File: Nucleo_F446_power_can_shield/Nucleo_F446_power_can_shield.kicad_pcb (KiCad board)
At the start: 2 copper layers, 70 x 59 mm, 2 parts, among them CN10 Conn_02x19_Odd_Even, CN7 Conn_02x19_Odd_Even

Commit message: commit
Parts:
- removed CN10, CN7: Conn_02x19_Odd_Even, Connector_PinSocket_2.54mm:PinSocket_2x19_P2.54mm_Vertical
- added J1: ISOCAN1, Connector_Molex:Molex_Micro-Fit_3.0_43045-0400_2x02_P3.00mm_Horizontal, F.Cu at (71.4, 55.0)
- added J10: ISOCAN2, Connector_Molex:Molex_Micro-Fit_3.0_43045-0400_2x02_P3.00mm_Horizontal, F.Cu at (128.1, 34.8)
- added J11: CAN1, Connector_Molex:Molex_Micro-Fit_3.0_43045-0400_2x02_P3.00mm_Horizontal, F.Cu at (74.2, 112.0)
- added J12: CAN2, Connector_Molex:Molex_Micro-Fit_3.0_43045-0400_2x02_P3.00mm_Horizontal, F.Cu at (116.8, 110.8)
- added J13: ISOCAN1, Connector_Molex:Molex_Micro-Fit_3.0_43045-0400_2x02_P3.00mm_Horizontal, F.Cu at (110.8, 33.6)
- added J14: ISOCAN2, Connector_Molex:Molex_Micro-Fit_3.0_43045-0400_2x02_P3.00mm_Horizontal, F.Cu at (159.2, 62.5)
- added J15: CAN1, Connector_Molex:Molex_Micro-Fit_3.0_43045-0400_2x02_P3.00mm_Horizontal, F.Cu at (101.0, 111.6)
- added J16: CAN2, Connector_Molex:Molex_Micro-Fit_3.0_43045-0400_2x02_P3.00mm_Horizontal, F.Cu at (141.3, 110.8)
- added J17: RJ45, Connector_RJ:RJ45_Amphenol_RJHSE5380, F.Cu at (70.1, 39.1)
- added J18: RJ45, Connector_RJ:RJ45_Amphenol_RJHSE5380, F.Cu at (162.1, 30.6)
- added J19: I2C3, Connector_PinHeader_2.54mm:PinHeader_1x04_P2.54mm_Vertical, F.Cu at (157.1, 86.5)
- added J2: ISOCAN2, Connector_Molex:Molex_Micro-Fit_3.0_43045-0400_2x02_P3.00mm_Horizontal, F.Cu at (140.4, 34.4)
- added J20: UART4, Connector_PinHeader_2.54mm:PinHeader_1x04_P2.54mm_Vertical, F.Cu at (76.5, 79.5)
- added J3: CAN1, Connector_Molex:Molex_Micro-Fit_3.0_43045-0400_2x02_P3.00mm_Horizontal, F.Cu at (71.2, 67.2)
- added J4: CAN2, Connector_Molex:Molex_Micro-Fit_3.0_43045-0400_2x02_P3.00mm_Horizontal, F.Cu at (154.6, 110.8)
- added J5: ISOCAN1, Connector_Molex:Molex_Micro-Fit_3.0_43045-0400_2x02_P3.00mm_Horizontal, F.Cu at (84.9, 33.4)
- added J6: ISOCAN2, Connector_Molex:Molex_Micro-Fit_3.0_43045-0400_2x02_P3.00mm_Horizontal, F.Cu at (159.0, 49.0)
- added J7: CAN1, Connector_Molex:Molex_Micro-Fit_3.0_43045-0400_2x02_P3.00mm_Horizontal, F.Cu at (87.6, 111.9)
- added J8: CAN2, Connector_Molex:Molex_Micro-Fit_3.0_43045-0400_2x02_P3.00mm_Horizontal, F.Cu at (128.8, 110.9)
- added J9: ISOCAN1, Connector_Molex:Molex_Micro-Fit_3.0_43045-0400_2x02_P3.00mm_Horizontal, F.Cu at (97.9, 33.6)
- added M1: Isolated-Can-Transceiver-Module-ISO1050-Module, PolyuRobotics:Isolated-Can-Transceiver-Module-ISO1050-Module, F.Cu at (105.4, 58.8)
- added M2: Isolated-Can-Transceiver-Module-ISO1050-Module, PolyuRobotics:Isolated-Can-Transceiver-Module-ISO1050-Module, F.Cu at (124.3, 59.0)
- added M3: TJA1050_Module, PolyuRobotics:TJA1050_CAN_Module, F.Cu at (101.4, 89.6)
- added M4: TJA1050_Module, PolyuRobotics:TJA1050_CAN_Module, F.Cu at (130.5, 89.1)
- added U1: NUCLEO-F446RE, NUCLEO-F446RE:MODULE_NUCLEO-F446RE, F.Cu at (115.6, 65.3)
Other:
- board outline removed
- net class Default removed
- board text removed: "STM32 Morpho"
- board text removed: "®©®"

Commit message: shield
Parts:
- added C1: 16v220uF, Capacitor_SMD:C_Elec_6.3x7.7, F.Cu at (86.2, 104.5)
- added C2: 16v 220uF, Capacitor_SMD:C_Elec_6.3x7.7, F.Cu at (190.3, 84.6)
- added C3: 50v 47uF, Capacitor_SMD:C_Elec_6.3x7.7, F.Cu at (88.1, 64.1)
- added C4: 16v 220uF, Capacitor_SMD:C_Elec_6.3x7.7, F.Cu at (86.4, 114.5)
- added J21: xt60 male, PolyuRobotics:XT60PW-M20, F.Cu at (87.5, 47.0)
- added U2: MP1584, PolyuRobotics:DC-DC-mp1584_module, F.Cu at (78.4, 72.2)
- U1: footprint NUCLEO-F446RE:MODULE_NUCLEO-F446RE -> PolyuRobotics:NUCLEO-F446RE
- moved J3 145.1 mm to (202.9, 128.2), turned to -90 degrees
- moved J11 128.6 mm to (202.8, 116.1), turned to -90 degrees
- moved J7 115.5 mm to (202.7, 102.7), turned to -90 degrees
- moved J17 106.9 mm to (176.9, 43.4), turned to 0 degrees
- moved J15 103.8 mm to (202.4, 89.3), turned to -90 degrees
- moved J18 100.0 mm to (184.1, 128.1), turned to 180 degrees
- moved J10 95.3 mm to (152.7, 126.8), turned to 180 degrees
- moved J12 92.4 mm to (202.7, 76.8), turned to -90 degrees
- moved J2 92.3 mm to (140.1, 126.8), turned to 180 degrees
- moved J8 87.1 mm to (202.6, 64.6), turned to -90 degrees
- moved J4 86.5 mm to (202.7, 39.0), turned to -90 degrees
- moved J16 84.9 mm to (202.7, 52.3), turned to -90 degrees
- moved J6 83.7 mm to (127.8, 126.7), turned to 180 degrees
- moved M3 79.4 mm to (180.0, 100.6)
- moved J14 77.6 mm to (115.8, 126.8), turned to 180 degrees
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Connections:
- M1 pad 6: /ISO-CAN1H+ -> /ISO-CAN1+
- M1 pad 7: /ISO-CAN1H- -> /ISO-CAN1-
- U1 pad CN10_32: GND -> unconnected-(U1-PadCN10_32)
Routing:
- net +5V: track 0.00 -> 176.3 mm, vias 0 -> 2
- net <NO NET>: track 0.00 -> 173.7 mm, vias 0 -> 2
- net /ISO-CAN2-: track 0.00 -> 135.7 mm, vias 0 -> 1
- net /ISO-CAN2+: track 0.00 -> 131.9 mm, vias 0 -> 1
- net /ISO-CAN1+: track 0.00 -> 101.3 mm
- net /ISO-CAN1-: track 0.00 -> 95.8 mm
- net /PB4: track 0.00 -> 83.2 mm
- net /PB5: track 0.00 -> 82.7 mm
- net /PA8: track 0.00 -> 81.2 mm
- net VCC: track 0.00 -> 77.1 mm, vias 0 -> 1
- net /CAN1-: track 0.00 -> 75.1 mm
- net /CAN2-: track 0.00 -> 74.2 mm
- net /CAN2+: track 0.00 -> 72.5 mm
- net /CAN1+: track 0.00 -> 71.8 mm
- net +3V3: track 0.00 -> 69.9 mm
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- added copper zone on B.Cu, net GND
- added copper zone on F.Cu, net GND
- added copper zone on B.Cu, net GND1
- added copper zone on F.Cu, net GND1
- added copper zone on B.Cu, net GND2
- added copper zone on F.Cu, net GND2
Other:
- board outline added: 139.7 x 104.8 mm

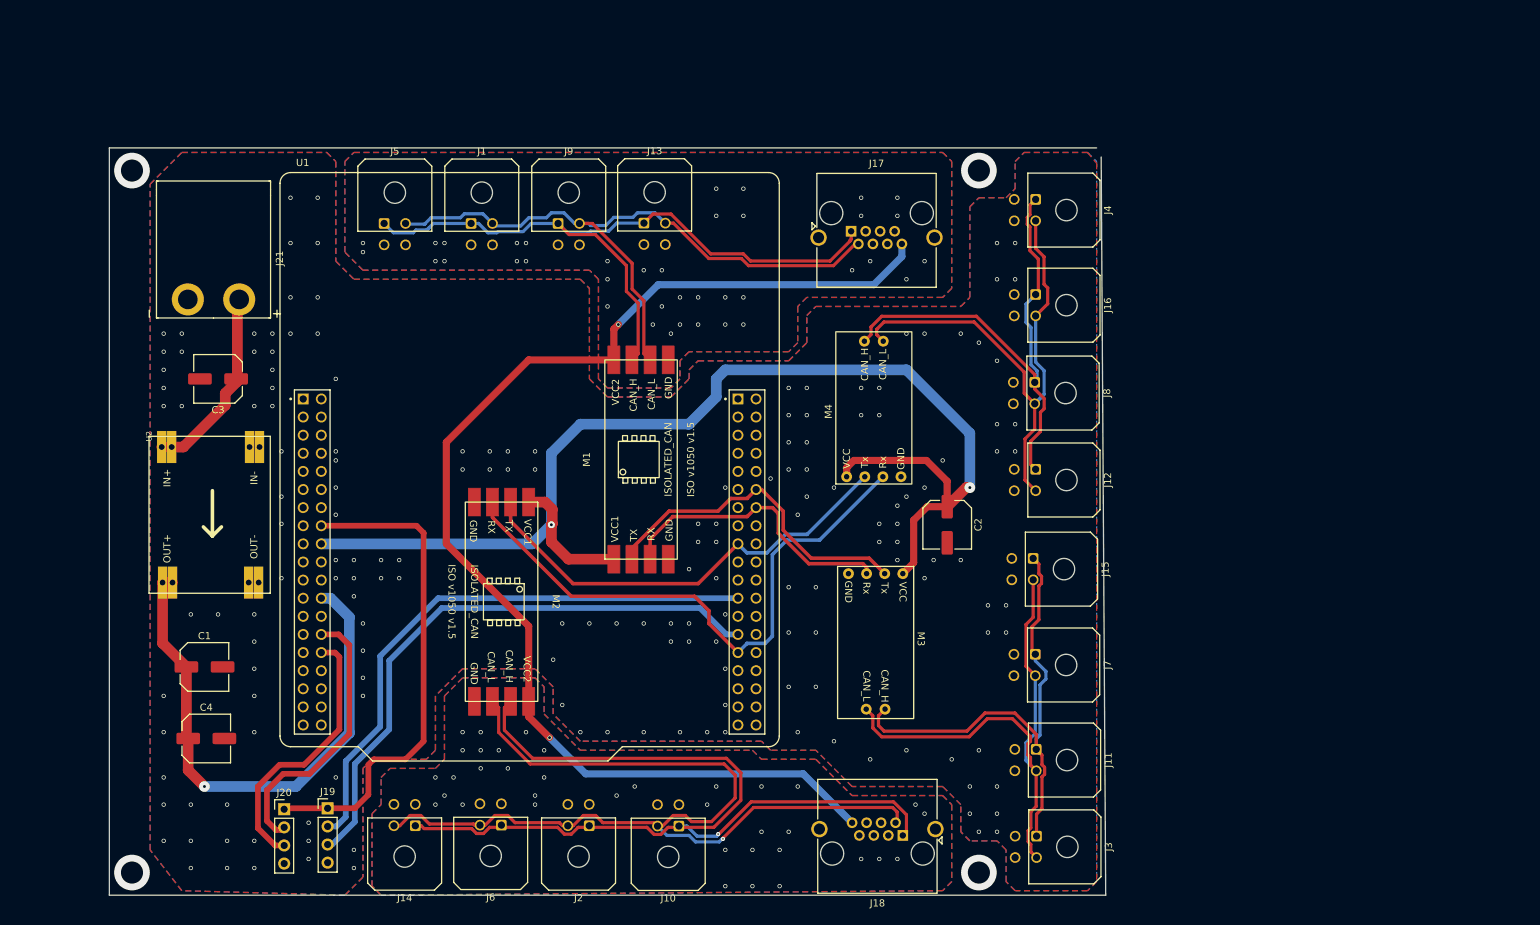
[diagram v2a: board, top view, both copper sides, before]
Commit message: add bullyU
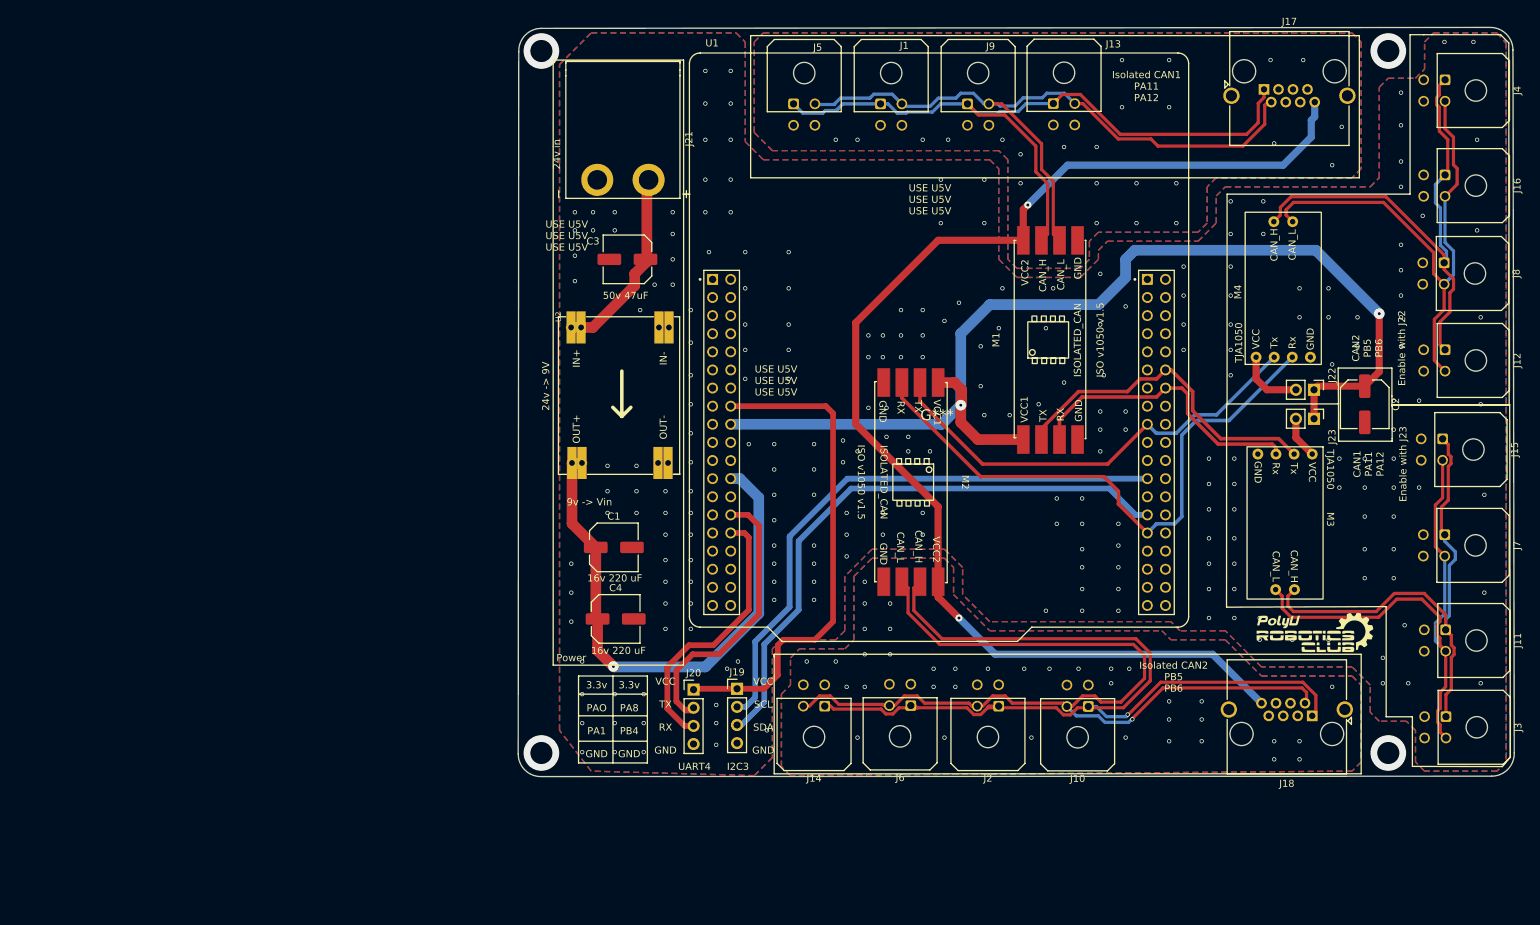
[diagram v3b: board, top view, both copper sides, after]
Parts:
- added G***: LOGO, PolyuRobotics:Club_logo, F.Cu at (242.0, 99.9)
- added G***: LOGO, PolyuRobotics:BullyU_logo, B.Cu at (188.9, 69.2)
- added G***: LOGO, PolyuRobotics:Club_logo, B.Cu at (214.6, 37.3)
- added J22: enable, Connector_PinHeader_2.54mm:PinHeader_1x02_P2.54mm_Vertical, F.Cu at (241.8, 65.6)
- added J23: enable, Connector_PinHeader_2.54mm:PinHeader_1x02_P2.54mm_Vertical, F.Cu at (241.8, 69.7)
- moved J17 61.2 mm to (234.7, 23.5)
- moved C2 60.9 mm to (248.9, 67.7)
- moved J14 59.8 mm to (173.2, 110.0)
- moved J21 59.8 mm to (144.9, 30.2)
- moved J6 59.8 mm to (185.2, 109.9)
- moved M2 59.8 mm to (185.2, 78.6)
- moved C1 59.8 mm to (143.6, 87.7)
- moved C3 59.8 mm to (145.5, 47.4)
- moved C4 59.8 mm to (143.8, 97.8)
- moved J1 59.8 mm to (181.0, 25.6)
- moved J10 59.8 mm to (210.1, 110.0)
- moved J11 59.8 mm to (260.2, 99.3)
- moved J12 59.8 mm to (260.1, 60.0)
- moved J13 59.8 mm to (205.2, 25.5)
- moved J15 59.8 mm to (259.8, 72.5)
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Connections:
- M3 pad 1: +5V -> Net-(M3-Pad1)
- M4 pad 1: +5V -> Net-(M4-Pad1)
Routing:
- net +5V: track 176.3 -> 152.6 mm
- net Net-(M4-Pad1): track 0.00 -> 9.27 mm
- net Net-(M3-Pad1): track 0.00 -> 5.90 mm
- net /ISO-CAN1-: track 95.8 -> 99.1 mm
- net <NO NET>: track 173.7 -> 177.1 mm
- net /ISO-CAN2+: track 131.9 -> 134.6 mm
- net /ISO-CAN1+: track 101.3 -> 103.8 mm
- net GND2: vias 0 -> 37
- net GND1: vias 0 -> 24
- net GND: vias 0 -> 239
- net (no net): vias 248 -> 4
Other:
- board size 139.7 x 104.8 mm -> 139.7 x 105 mm
- board text added: "16v 220 uF"
- board text added: "24v -> 9V"
- board text added: "24v in"
- board text added: "3.3v PA8 PB4 GND"
- board text added: "3.3v PAO PA1 GND"
- board text added: "50v 47uF"
- board text added: "9v -> Vin"
- board text added: "CAN1 PA11 PA12 Enable with J23"
- board text added: "CAN2 PB5 PB6 Enable with J22"
- board text added: "I2C3"
- board text added: "Isolated / non Isolated CAN1: PA11, PA12 Isolated / non Isolated CAN2: PB5, PB6 UART3: PA0, PA1 I2C3: PA8, PB4"
- board text added: "Isolated CAN1 PA11 PA12"
- board text added: "Isolated CAN2 PB5 PB6"
- board text added: "Necleo CAN Board Rev 1.0 By SamsonChau For F446RE"
- board text added: "Power"
- board text added: "TJA1050"
- board text added: "UART4"
- board text added: "USE U5V USE U5V USE U5V"
- board text added: "Use on can tranceiver on each channel only"
- board text added: "VCC SCL SDA GND"
- board text added: "VCC TX RX GND"

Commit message: add bullyU
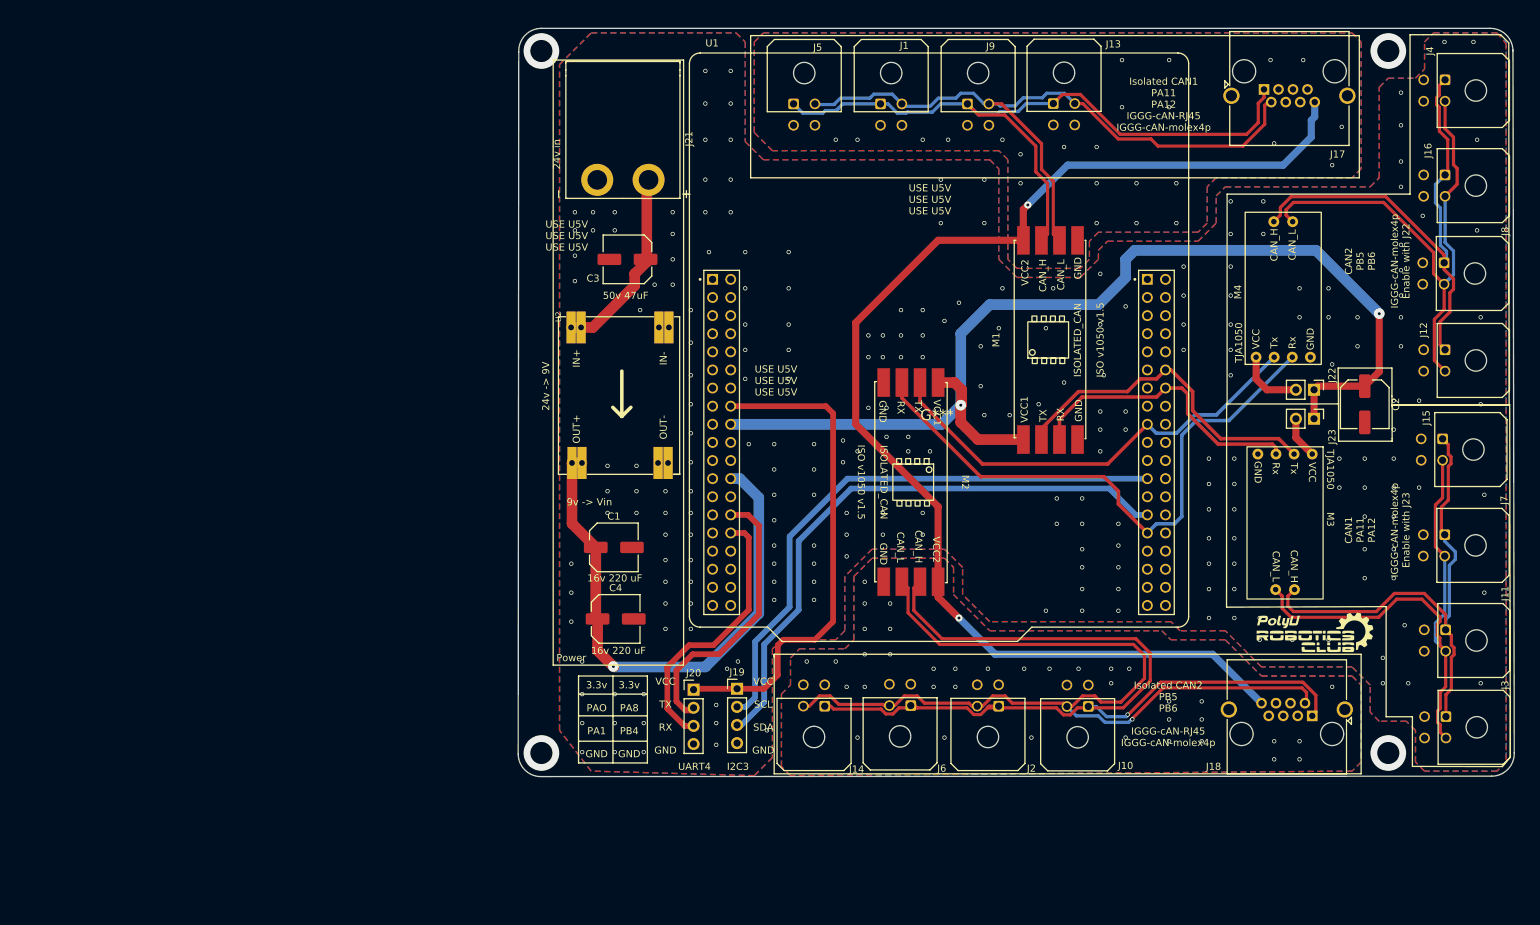
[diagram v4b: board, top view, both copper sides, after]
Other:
- board size 139.7 x 105 mm -> 139.7 x 104.9 mm
- rule pad_to_mask_clearance: 0.2 -> 0
- board text added: "Add Tape Here"
- board text added: "CAN1 PA11 PA12 IGGG-cAN-molex4p Enable with J23"
- board text added: "CAN2 PB5 PB6 IGGG-cAN-molex4p Enable with J22"
- board text added: "Isolated CAN1 PA11 PA12 IGGG-cAN-RJ45 IGGG-cAN-molex4p"
- board text added: "Isolated CAN2 PB5 PB6 IGGG-cAN-RJ45 IGGG-cAN-molex4p"
- board text removed: "CAN1 PA11 PA12 Enable with J23"
- board text removed: "CAN2 PB5 PB6 Enable with J22"
- board text removed: "Isolated CAN1 PA11 PA12"
- board text removed: "Isolated CAN2 PB5 PB6"

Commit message: change
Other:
- board text removed: "USE U5V USE U5V USE U5V"
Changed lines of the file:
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@@
     (effects (font (size 1 1) (thickness 0.15)) (justify left mirror))
-  )
-  (gr_text "USE U5V\nUSE U5V\nUSE U5V" (at 246.205 54.595) (layer "B.SilkS")
-    (effects (font (size 1 1) (thickness 0.15)) (justify mirror))
   )
   (gr_text "Add Tape Here" (at 144.224 65.517) (layer "B.SilkS")
@@
     (effects (font (size 1 1) (thickness 0.15)))
   )
-  (gr_text "USE U5V\nUSE U5V\nUSE U5V" (at 187.912 38.974) (layer "F.SilkS")
-    (effects (font (size 1 1) (thickness 0.15)))
-  )
   (gr_text "9v -> Vin" (at 140.16 81.392) (layer "F.SilkS")
     (effects (font (size 1 1) (thickness 0.15)))
   )
   (gr_text "UART4" (at 154.892 118.476) (layer "F.SilkS")
-    (effects (font (size 1 1) (thickness 0.15)))
-  )
-  (gr_text "USE U5V\nUSE U5V\nUSE U5V" (at 136.985 44.054) (layer "F.SilkS")
     (effects (font (size 1 1) (thickness 0.15)))
   )
@@
     (effects (font (size 1 1) (thickness 0.15)))
   )
-  (gr_text "USE U5V\nUSE U5V\nUSE U5V" (at 166.322 64.374) (layer "F.SilkS")
-    (effects (font (size 1 1) (thickness 0.15)))
-  )

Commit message: oh
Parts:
- added D1: can_led, LED_SMD:LED_0805_2012Metric_Pad1.15x1.40mm_HandSolder, F.Cu at (231.1, 34.5)
- added D2: can_led, LED_SMD:LED_0805_2012Metric_Pad1.15x1.40mm_HandSolder, F.Cu at (223.2, 103.9)
- added D3: power_led, LED_SMD:LED_0805_2012Metric_Pad1.15x1.40mm_HandSolder, F.Cu at (150.3, 93.3)
- added D4: can_led, LED_SMD:LED_0805_2012Metric_Pad1.15x1.40mm_HandSolder, F.Cu at (227.3, 91.9)
- added D5: can_led, LED_SMD:LED_0805_2012Metric_Pad1.15x1.40mm_HandSolder, F.Cu at (227.3, 57.8)
- added J24: enable, Connector_PinHeader_2.54mm:PinHeader_1x02_P2.54mm_Vertical, F.Cu at (171.3, 42.0)
- added J25: enable, Connector_PinHeader_2.54mm:PinHeader_1x02_P2.54mm_Vertical, F.Cu at (165.6, 42.0)
- added R1: 10K, Resistor_SMD:R_0805_2012Metric_Pad1.20x1.40mm_HandSolder, F.Cu at (192.6, 39.2)
- added R2: 10K, Resistor_SMD:R_0805_2012Metric_Pad1.20x1.40mm_HandSolder, F.Cu at (199.7, 95.1)
- added R3: 10K, Resistor_SMD:R_0805_2012Metric_Pad1.20x1.40mm_HandSolder, F.Cu at (150.3, 83.8)
- added R4: 10K, Resistor_SMD:R_0805_2012Metric_Pad1.20x1.40mm_HandSolder, F.Cu at (227.3, 87.0)
- added R5: 10K, Resistor_SMD:R_0805_2012Metric_Pad1.20x1.40mm_HandSolder, F.Cu at (227.3, 63.0)
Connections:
- M1 pad 1: +5V -> Net-(M1-Pad1)
- M2 pad 1: +5V -> Net-(M2-Pad1)
- M2 pad 5: <NO NET> -> (no net)
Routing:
- net Net-(M2-Pad1): track 0.00 -> 88.9 mm
- net <NO NET>: track 177.1 -> 107.7 mm
- net Net-(M1-Pad1): track 0.00 -> 64.3 mm
- net Net-(D1-Pad2): track 0.00 -> 61.0 mm
- net Net-(D2-Pad2): track 0.00 -> 25.2 mm
- net Net-(M3-Pad1): track 5.90 -> 25.6 mm
- net +5V: track 152.6 -> 171.1 mm, vias 2 -> 1
- net GND: track 0.00 -> 12.9 mm, vias 239 -> 221
- net Net-(D3-Pad2): track 0.00 -> 7.52 mm
- net Net-(D4-Pad2): track 0.00 -> 2.93 mm

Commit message: diode
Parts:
- added D6: ss24, Diode_SMD:D_SMB-SMC_Universal_Handsoldering, F.Cu at (150.3, 46.3)
- added D7: SMBJ24CA, Diode_SMD:D_SMB-SMC_Universal_Handsoldering, F.Cu at (140.2, 43.8)
- moved R3 7.86 mm to (150.3, 91.6), turned to 0 degrees
- moved C3 6.71 mm to (140.2, 51.4)
- moved U2 2.79 mm to (135.8, 58.2)
- moved D3 1.26 mm to (150.3, 94.6), turned to 180 degrees
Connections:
- C3 pad 1: +24V -> Net-(C3-Pad1)
- M2 pad 5: (no net) -> <NO NET>
- U2 pad IN1+: +24V -> Net-(C3-Pad1)
- U2 pad IN2+: +24V -> Net-(C3-Pad1)
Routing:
- net Net-(C3-Pad1): track 0.00 -> 18.2 mm
- net +24V: track 26.9 -> 14.9 mm
- net +5V: track 171.1 -> 179.7 mm
- net Net-(D3-Pad2): track 7.52 -> 3.79 mm
- net VCC: track 77.1 -> 74.4 mm
- net GND: vias 221 -> 208

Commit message: add diode
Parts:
- added D8: SMBJ9VCA, Diode_SMD:D_SMB-SMC_Universal_Handsoldering, F.Cu at (144.7, 85.5)
- added R6: 4.7k, Resistor_SMD:R_0805_2012Metric_Pad1.20x1.40mm_HandSolder, F.Cu at (168.6, 94.6)
- added R7: 4.7k, Resistor_SMD:R_0805_2012Metric_Pad1.20x1.40mm_HandSolder, F.Cu at (172.2, 94.6)
- R3: value 10K -> 22K
- moved R3 18.0 mm to (140.7, 106.8)
- moved D3 13.0 mm to (145.7, 106.8)
- moved C1 9.06 mm to (140.2, 96.1), turned to -90 degrees
- moved D7 7.55 mm to (145.7, 38.7)
- moved C3 5.23 mm to (144.7, 54.0), turned to 0 degrees
- moved D6 4.57 mm to (145.7, 46.3), turned to 0 degrees
- moved J21 4.39 mm to (145.5, 25.9)
- moved C4 4.27 mm to (147.8, 96.1), turned to -90 degrees
- moved J19 1.91 mm to (159.0, 107.6)
- moved J20 0.13 mm to (154.8, 107.6)
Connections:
- R3 pad 1: +5V -> VCC
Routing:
- net VCC: track 74.4 -> 107.7 mm
- net +5V: track 179.7 -> 152.3 mm
- net /PB4: track 83.2 -> 101.4 mm
- net /PA8: track 81.2 -> 95.8 mm
- net Net-(J22-Pad2): track 9.27 -> 18.3 mm
- net GND: track 12.9 -> 21.0 mm, vias 208 -> 190
- net +3V3: track 69.9 -> 66.7 mm
- net Net-(D5-Pad2): track 0.00 -> 3.18 mm
- net Net-(C3-Pad1): track 18.2 -> 17.1 mm
- net /PB5: track 82.7 -> 83.6 mm
- net /PA0: track 39.2 -> 38.5 mm
- net Net-(D3-Pad2): track 3.79 -> 3.03 mm
- net /PA1: track 38.2 -> 37.5 mm
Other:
- board text added: "22K"
- board text added: "3.3v SCL SDA GND"
- board text added: "3.3v TX RX GND"
- board text added: "4.7k"
- board text added: "9v <- 24v"
- board text added: "Power_led"
- board text added: "SMBJ24CA"
- board text added: "SMBJ9vCA"
- board text added: "ss24"
- board text removed: "24v -> 9V"
- board text removed: "VCC SCL SDA GND"
- board text removed: "VCC TX RX GND"
